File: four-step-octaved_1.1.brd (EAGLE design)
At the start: 93.7 x 43.2 mm, 39 parts, among them IC1 556, IC2 4017N, IC3 4040N, J1 BATTERY, J2 SPEAKER, U1 LM386N

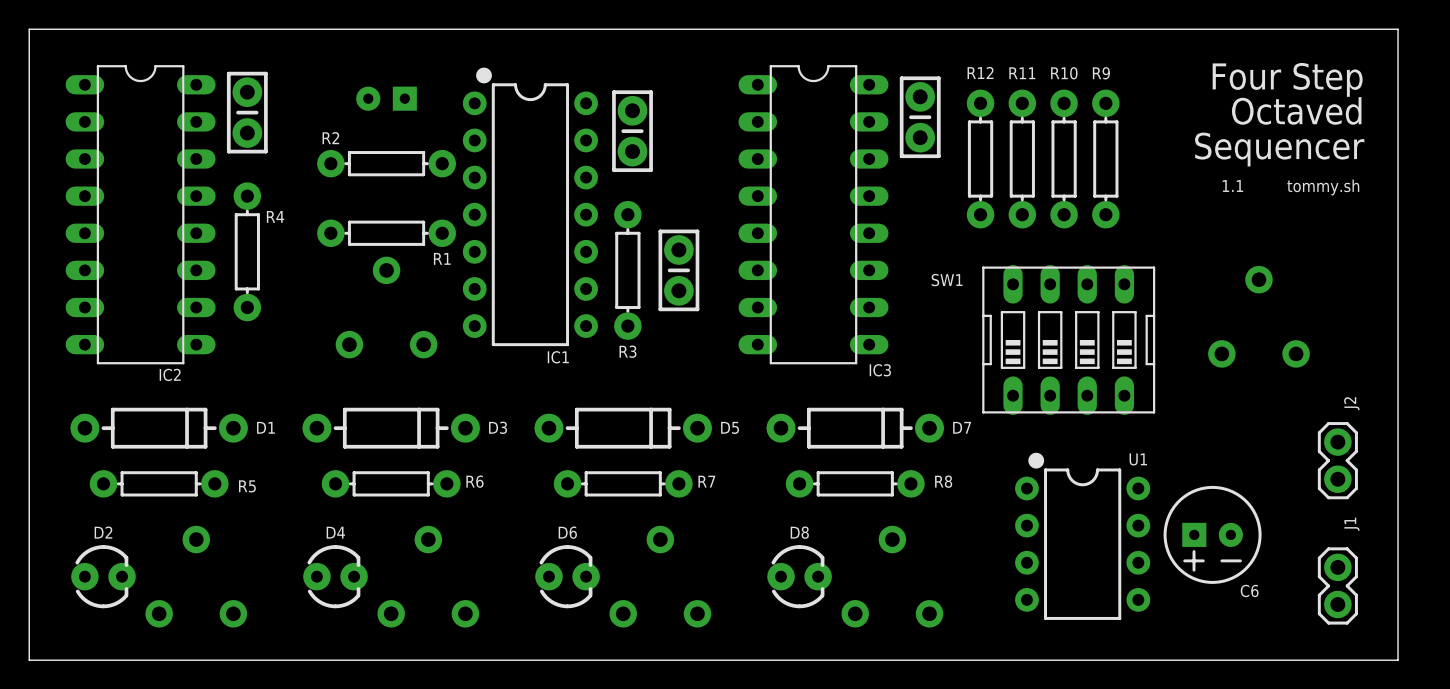
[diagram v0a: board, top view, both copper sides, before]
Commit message: Reorganize board
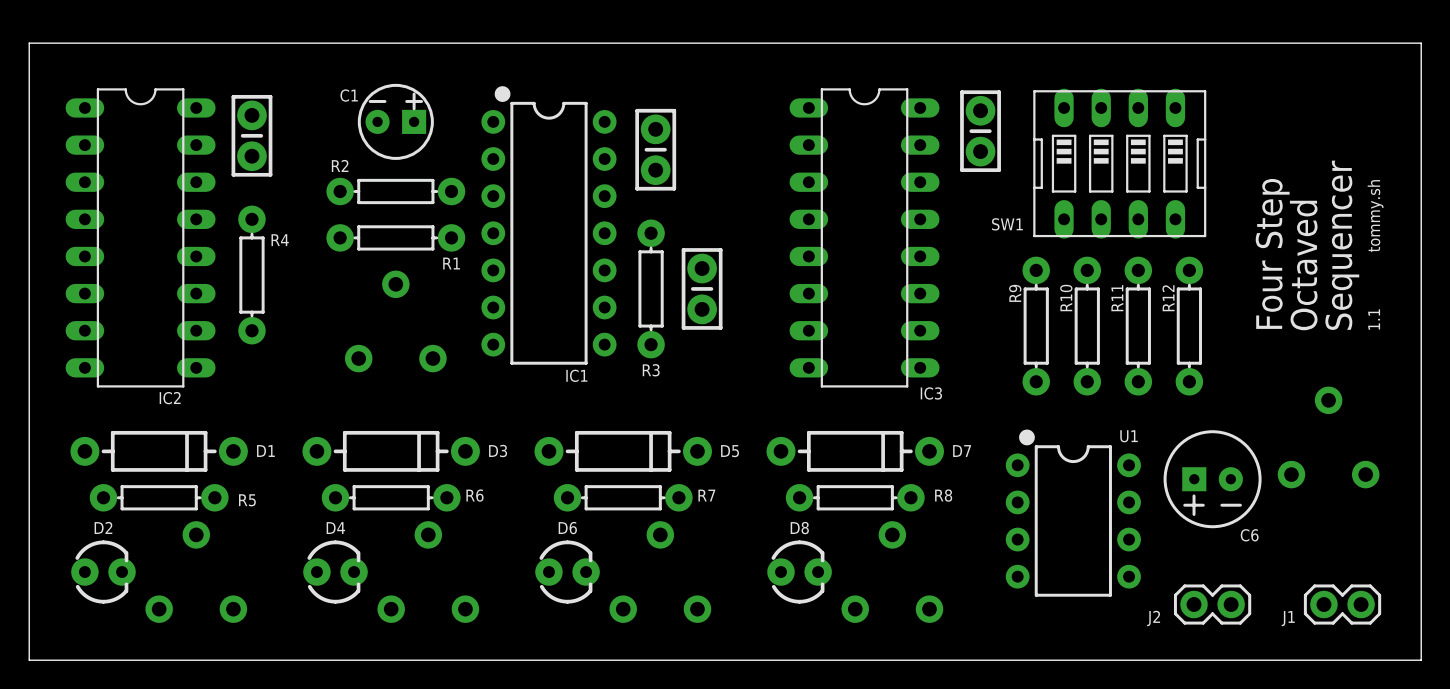
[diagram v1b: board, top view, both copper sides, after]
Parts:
- moved RV6 65.1 mm to (88.9, 12.7)
- moved RV1 59.1 mm to (25.1, 20.6)
- moved R12 18.3 mm to (79.4, 22.9), turned to 270 degrees
- moved R11 13.9 mm to (75.9, 22.9), turned to 270 degrees
- moved J2 13.3 mm to (82.2, 3.81), turned to 180 degrees
- moved SW1 12.6 mm to (74.6, 34.0), turned to 180 degrees
- moved R9 12.4 mm to (68.9, 22.9), turned to 270 degrees
- moved R10 11.5 mm to (72.4, 22.9), turned to 270 degrees
- moved C5 4.24 mm to (65.1, 36.2)
- moved IC3 3.84 mm to (57.1, 28.9)
- moved C6 3.81 mm to (81.0, 12.4)
- moved J1 3.00 mm to (91.1, 3.81), turned to 180 degrees
- moved C2 2.03 mm to (42.9, 34.9)
- moved C3 2.03 mm to (46.0, 25.4)
- moved R3 2.03 mm to (42.5, 25.4)
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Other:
- board size 93.7 x 43.2 mm -> 95.2 x 42.2 mm

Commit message: Fix missing 556 pin10 on both schematics
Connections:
- net +9V: now also IC1.10
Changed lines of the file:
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@@
 <contactref element="C5" pad="1"/>
 <contactref element="J1" pad="1"/>
+<contactref element="IC1" pad="10"/>
 <wire x1="60.96" y1="37.7825" x2="65.0875" y2="37.592" width="0" layer="19" extent="1-1"/>
 <wire x1="42.8625" y1="36.322" x2="60.96" y2="37.7825" width="0" layer="19" extent="1-1"/>
 <wire x1="39.37" y1="36.83" x2="42.8625" y2="36.322" width="0" layer="19" extent="1-1"/>
-<wire x1="31.75" y1="29.21" x2="39.37" y2="36.83" width="0" layer="19" extent="1-1"/>
+<wire x1="39.37" y1="26.67" x2="39.37" y2="36.83" width="0" layer="19" extent="1-1"/>
+<wire x1="31.75" y1="29.21" x2="39.37" y2="26.67" width="0" layer="19" extent="1-1"/>
 <wire x1="21.2725" y1="28.8925" x2="31.75" y2="29.21" width="0" layer="19" extent="1-1"/>
 <wire x1="15.24" y1="37.2745" x2="21.2725" y2="28.8925" width="0" layer="19" extent="1-1"/>

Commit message: Route 1.1
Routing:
- net GND: track 0.00 -> 230.3 mm
- net +9V: track 0.00 -> 131.0 mm
- net N$10: track 0.00 -> 82.5 mm
- net N$9: track 0.00 -> 77.3 mm
- net N$19: track 0.00 -> 71.1 mm
- net N$8: track 0.00 -> 51.0 mm
- net N$31: track 0.00 -> 38.1 mm
- net N$7: track 0.00 -> 33.4 mm
- net N$25: track 0.00 -> 31.7 mm
- net N$5: track 0.00 -> 30.0 mm
- net N$21: track 0.00 -> 26.1 mm
- net N$43: track 0.00 -> 25.7 mm
- net N$24: track 0.00 -> 25.2 mm
- net N$2: track 0.00 -> 24.9 mm
- net N$6: track 0.00 -> 24.6 mm
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
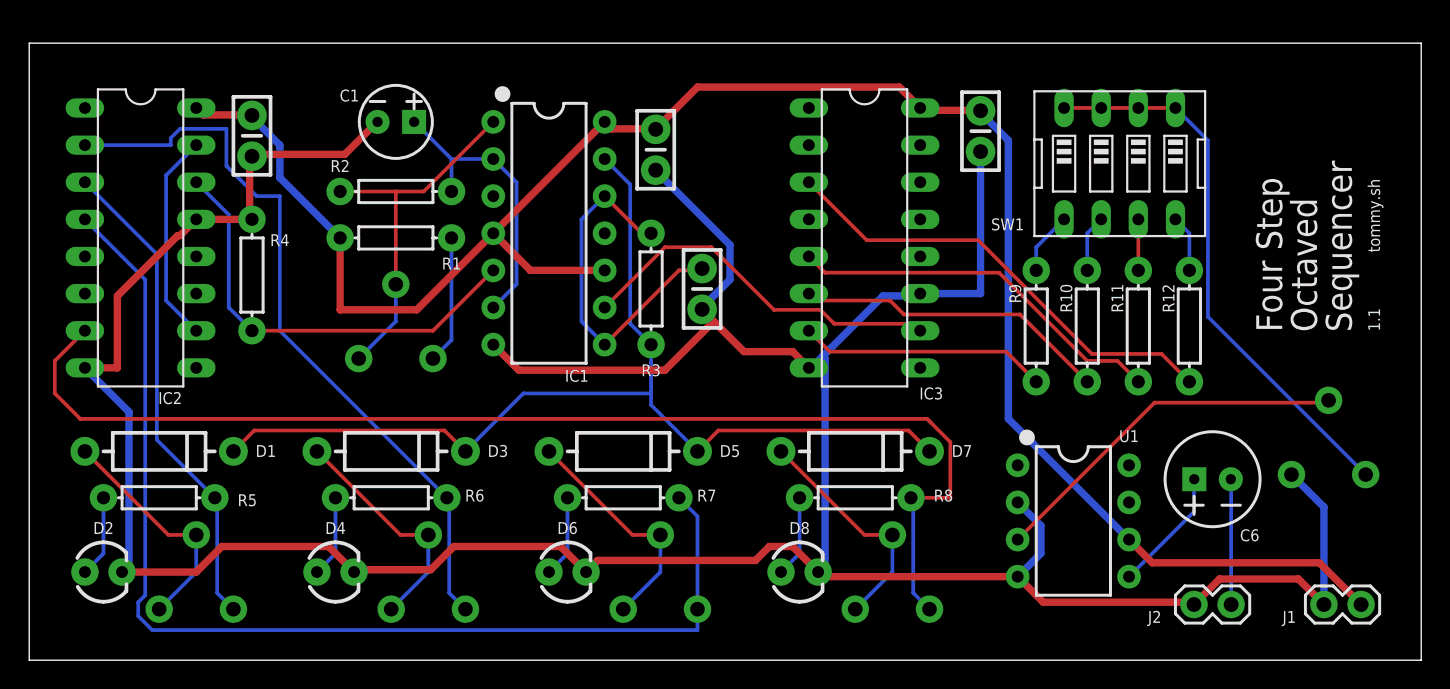
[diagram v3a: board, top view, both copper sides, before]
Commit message: Fix text on wrong layer, only on 1.1
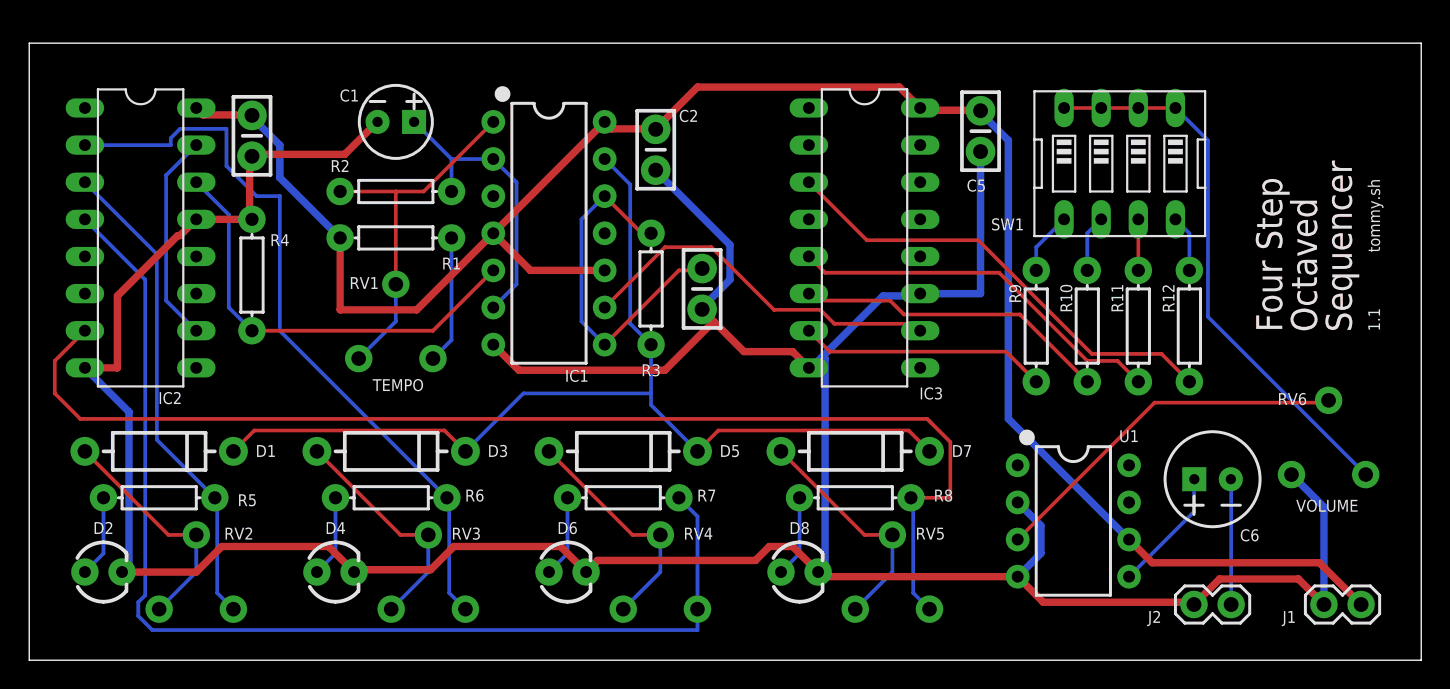
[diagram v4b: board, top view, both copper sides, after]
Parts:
- J1: value BATTERY -> -BATTERY+
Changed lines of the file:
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@@
 <text x="92.422521875" y="27.899253125" size="0.8128" layer="21" font="vector" ratio="10" rot="R90">tommy.sh</text>
 <text x="17.145" y="37.7825" size="0.8128" layer="23" font="vector">C4</text>
-<text x="44.45" y="36.83" size="0.8128" layer="23" font="vector">C2</text>
+<text x="44.45" y="36.83" size="0.8128" layer="21" font="vector">C2</text>
 <text x="45.4025" y="21.2725" size="0.8128" layer="23" font="vector">C3</text>
-<text x="21.9075" y="25.4" size="0.8128" layer="23" font="vector">RV1</text>
-<text x="85.4075" y="17.4625" size="0.8128" layer="23" font="vector">RV6</text>
-<text x="13.335" y="8.255" size="0.8128" layer="23" font="vector">RV2</text>
-<text x="28.8925" y="8.255" size="0.8128" layer="23" font="vector">RV3</text>
-<text x="60.6425" y="8.255" size="0.8128" layer="23" font="vector">RV5</text>
-<text x="44.7675" y="8.255" size="0.8128" layer="23" font="vector">RV4</text>
-<text x="64.135" y="32.0675" size="0.8128" layer="23" font="vector">C5</text>
-<text x="23.495" y="18.415" size="0.8128" layer="23" font="vector">TEMPO</text>
-<text x="86.6775" y="10.16" size="0.8128" layer="23" font="vector">VOLUME</text>
+<text x="21.9075" y="25.4" size="0.8128" layer="21" font="vector">RV1</text>
+<text x="85.4075" y="17.4625" size="0.8128" layer="21" font="vector">RV6</text>
+<text x="13.335" y="8.255" size="0.8128" layer="21" font="vector">RV2</text>
+<text x="28.8925" y="8.255" size="0.8128" layer="21" font="vector">RV3</text>
+<text x="60.6425" y="8.255" size="0.8128" layer="21" font="vector">RV5</text>
+<text x="44.7675" y="8.255" size="0.8128" layer="21" font="vector">RV4</text>
+<text x="64.135" y="32.0675" size="0.8128" layer="21" font="vector">C5</text>
+<text x="23.495" y="18.415" size="0.8128" layer="21" font="vector">TEMPO</text>
+<text x="86.6775" y="10.16" size="0.8128" layer="21" font="vector">VOLUME</text>
 <text x="92.422521875" y="22.501753125" size="0.8128" layer="21" font="vector" ratio="10" rot="R90">1.1</text>
+<text x="90.48991875" y="22.450925" size="1.778" layer="1" font="vector" ratio="15" distance="34" rot="R90">Four Step
+Octaved
+Sequencer</text>
 </plain>
 <attributes>
@@
 <attribute name="NAME" x="60.8965" y="17.8435" size="0.8128" layer="25" font="vector"/>
 </element>
-<element name="J1" library="SparkFun-Connectors" package="1X02" value="BATTERY" x="91.1225" y="3.81" smashed="yes" rot="R180">
+<element name="J1" library="SparkFun-Connectors" package="1X02" value="-BATTERY+" x="91.1225" y="3.81" smashed="yes" rot="R180">
 <attribute name="NAME" x="86.6775" y="3.3655" size="0.8128" layer="25" font="vector" rot="R180"/>
 <attribute name="VALUE" x="92.3925" y="6.477" size="0.8128" layer="27" font="vector" rot="R180"/>
